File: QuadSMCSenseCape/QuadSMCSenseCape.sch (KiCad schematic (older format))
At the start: 16 parts, among them P8 BeagleBone_Black_Header, P9 BeagleBone_Black_Header, T1 Motor 1, T2 Motor 2, T3 Motor 3, T4 Motor 4, U1 TC4428, U2 TC4428, U3 TC4428, U4 TC4428, U5 74HCT00, U6 74HCT00

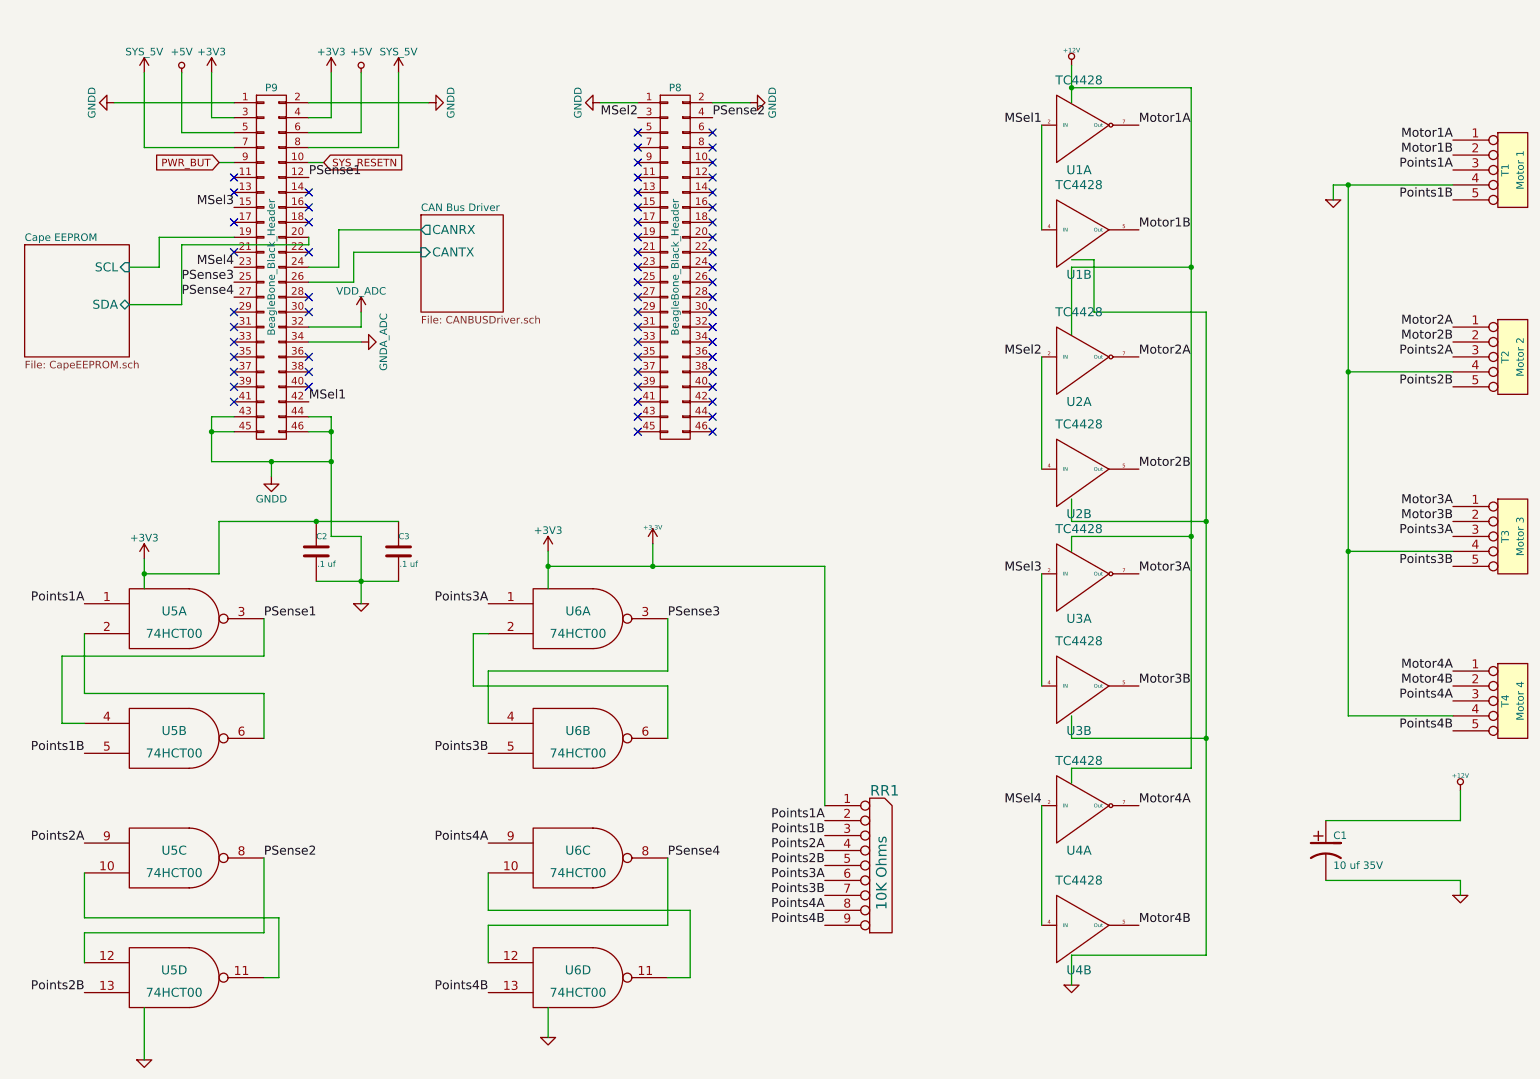
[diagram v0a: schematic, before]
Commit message: Remove CAN bus driver from QuadSMCSenseCape (delegate that to a dedicated Cape).
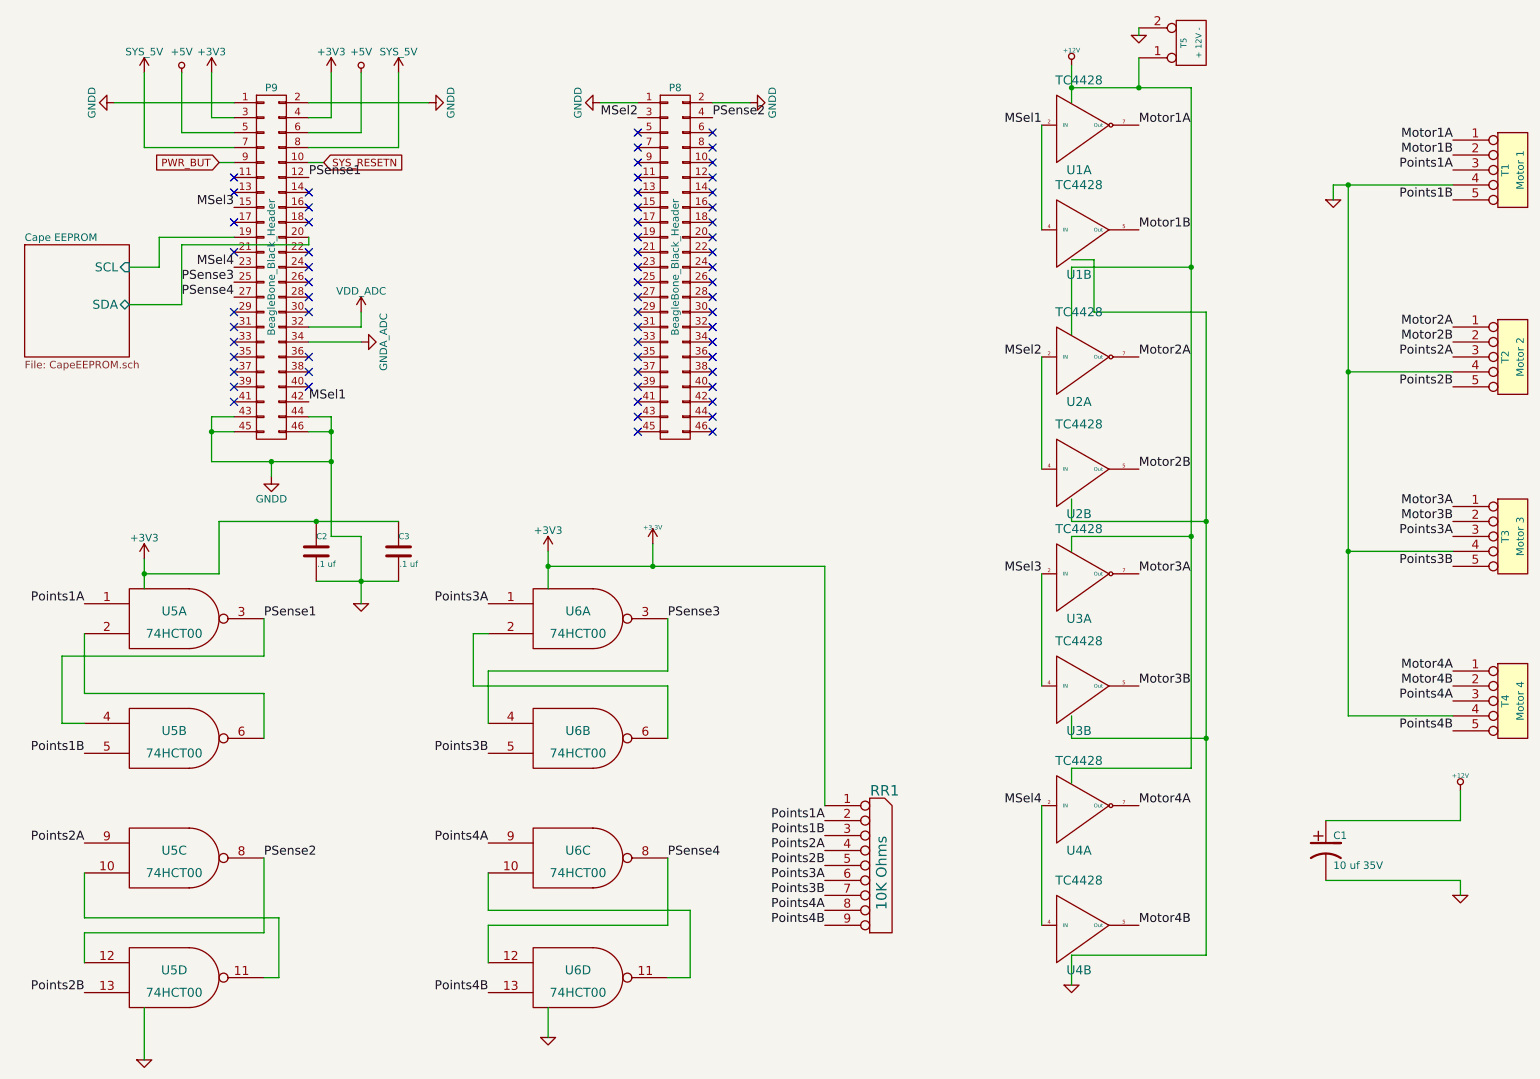
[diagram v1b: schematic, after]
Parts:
- added T5: + 12V -, symbol CONN_2
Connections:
- net +12V: now also T5.1 (P1)
- net GND: now also T5.2 (PM)
- net CAN Bus Driver/CANRX: no longer names the net of P9.24 (P24)
- net CAN Bus Driver/CANTX: no longer names the net of P9.26 (P26)
- no-connect marks 62 -> 64
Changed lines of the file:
@@
 $Descr A4 11693 8268
 encoding utf-8
-Sheet 1 3
+Sheet 1 2
 Title ""
-Date "3 feb 2019"
+Date "23 feb 2019"
 Rev ""
 Comp ""
@@
 	2850 3250 2850 4050
 Wire Wire Line
-	2850 3550 2050 3550
-Wire Wire Line
-	2050 3550 2050 3250
+	2050 3550 2850 3550
+Wire Wire Line
+	2050 3250 2050 3550
 Wire Wire Line
 	2050 3250 2200 3250
@@
 $EndComp
 Wire Wire Line
-	10350 1700 9550 1700
+	9550 1700 10350 1700
 Wire Wire Line
 	9550 1700 9550 1800
@@
 Text Label 6150 6650 2    60   ~ 0
 Points4B
-$Sheet
-S 3450 1900 550  650
-U 5C572C55
-F0 "CAN Bus Driver" 50
-F1 "CANBUSDriver.sch" 50
-F2 "CANTX" I L 3450 2150 60
-F3 "CANRX" O L 3450 2000 60
-$EndSheet
 Wire Wire Line
 	10400 5950 10400 5750
@@
 Text Label 5400 1250 0    60   ~ 0
 PSense2
-Wire Wire Line
-	3450 2000 2900 2000
-Wire Wire Line
-	2900 2000 2900 2250
-Wire Wire Line
-	2900 2250 2700 2250
-Wire Wire Line
-	3450 2150 3000 2150
-Wire Wire Line
-	3000 2150 3000 2350
-Wire Wire Line
-	3000 2350 2700 2350
 $Sheet
 S 800  2100 700  750
@@
 	1    0    0    -1
 $EndComp
+NoConn ~ 2700 2250
+NoConn ~ 2700 2350
+$Comp
+L CONN_2 T5
+U 1 1 5C7149FE
+P 8600 750
+F 0 "T5" V 8550 750 40  0000 C CNN
+F 1 "+ 12V -" V 8650 750 40  0000 C CNN
+F 2 "" H 8600 750 60  0000 C CNN
+F 3 "" H 8600 750 60  0000 C CNN
+	1    8600 750
+	1    0    0    1
+$EndComp
+Wire Wire Line
+	8250 850  8250 1050
+Connection ~ 8250 1050
+$Comp
+L GND #PWR025
+U 1 1 5C714AB7
+P 8250 700
+F 0 "#PWR025" H 8250 700 30  0001 C CNN
+F 1 "GND" H 8250 630 30  0001 C CNN
+F 2 "" H 8250 700 60  0000 C CNN
+F 3 "" H 8250 700 60  0000 C CNN
+	1    8250 700
+	1    0    0    -1
+$EndComp
+Wire Wire Line
+	8250 650  8250 700
 $EndSCHEMATC

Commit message: Create BOM for QuadSMCSenseCape.
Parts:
- C1: Mouser Part Number (none) -> 667-ECA-1HM100I
- C2, C3: Mouser Part Number (none) -> 581-SR201C104KARTR1
- P8, P9: Mouser Part Number (none) -> 200-ESQ12314GD
- RR1: Mouser Part Number (none) -> 652-4609X-1LF-10K
- T1, T2, T3, T4: Mouser Part Number (none) -> 651-1725685
- T5: Mouser Part Number (none) -> 651-1725656
- U1, U2, U3, U4: Mouser Part Number (none) -> 579-TC4428VPA
- U5, U6: Mouser Part Number (none) -> 595-SN74AHC00N
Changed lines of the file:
@@
 Sheet 1 2
 Title ""
-Date "23 feb 2019"
+Date "12 mar 2019"
 Rev ""
 Comp ""
@@
 F 2 "Socket_BeagleBone_Black:Socket_BeagleBone_Black" H 2450 1400 60  0001 C CNN
 F 3 "" H 2450 1400 60  0000 C CNN
+F 4 "200-ESQ12314GD " H 2450 2250 60  0001 C CNN "Mouser Part Number"
 	1    2450 2250
 	1    0    0    -1
@@
 F 2 "Socket_BeagleBone_Black:Socket_BeagleBone_Black" H 5150 1400 60  0001 C CNN
 F 3 "" H 5150 1400 60  0000 C CNN
+F 4 "200-ESQ12314GD " H 5150 2250 60  0001 C CNN "Mouser Part Number"
 	1    5150 2250
 	1    0    0    -1
@@
 F 2 "~" H 7850 1300 60  0000 C CNN
 F 3 "~" H 7850 1300 60  0000 C CNN
+F 4 "579-TC4428VPA" H 7850 1300 60  0001 C CNN "Mouser Part Number"
 	1    7850 1300
 	1    0    0    -1
@@
 F 2 "~" H 7850 2850 60  0000 C CNN
 F 3 "~" H 7850 2850 60  0000 C CNN
+F 4 "579-TC4428VPA" H 7850 2850 60  0001 C CNN "Mouser Part Number"
 	1    7850 2850
 	1    0    0    -1
@@
 F 2 "~" H 7850 3600 60  0000 C CNN
 F 3 "~" H 7850 3600 60  0000 C CNN
+F 4 "579-TC4428VPA" H 7850 3600 60  0001 C CNN "Mouser Part Number"
 	2    7850 3600
 	1    0    0    -1
@@
 F 2 "~" H 7850 4300 60  0000 C CNN
 F 3 "~" H 7850 4300 60  0000 C CNN
+F 4 "579-TC4428VPA" H 7850 4300 60  0001 C CNN "Mouser Part Number"
 	1    7850 4300
 	1    0    0    -1
@@
 F 2 "~" H 7850 5850 60  0000 C CNN
 F 3 "~" H 7850 5850 60  0000 C CNN
+F 4 "579-TC4428VPA" H 7850 5850 60  0001 C CNN "Mouser Part Number"
 	1    7850 5850
 	1    0    0    -1
@@
 F 2 "" H 10750 1600 60  0000 C CNN
 F 3 "" H 10750 1600 60  0000 C CNN
+F 4 "651-1725685" H 10750 1600 60  0001 C CNN "Mouser Part Number"
 	1    10750 1600
 	1    0    0    -1
@@
 F 2 "" H 10750 2850 60  0000 C CNN
 F 3 "" H 10750 2850 60  0000 C CNN
+F 4 "651-1725685" H 10750 2850 60  0001 C CNN "Mouser Part Number"
 	1    10750 2850
 	1    0    0    -1
@@
 F 2 "" H 10750 4050 60  0000 C CNN
 F 3 "" H 10750 4050 60  0000 C CNN
+F 4 "651-1725685" H 10750 4050 60  0001 C CNN "Mouser Part Number"
 	1    10750 4050
 	1    0    0    -1
@@
 F 2 "" H 10750 5150 60  0000 C CNN
 F 3 "" H 10750 5150 60  0000 C CNN
+F 4 "651-1725685" H 10750 5150 60  0001 C CNN "Mouser Part Number"
 	1    10750 5150
 	1    0    0    -1
@@
 F 2 "~" H 9500 6150 60  0000 C CNN
 F 3 "~" H 9500 6150 60  0000 C CNN
+F 4 "667-ECA-1HM100I" H 9500 6150 60  0001 C CNN "Mouser Part Number"
 	1    9500 6150
 	1    0    0    -1
@@
 F 2 "~" H 1800 4600 60  0000 C CNN
 F 3 "~" H 1800 4600 60  0000 C CNN
+F 4 "595-SN74AHC00N" H 1800 4600 60  0001 C CNN "Mouser Part Number"
 	1    1800 4600
 	1    0    0    -1
@@
 F 2 "~" H 4500 4600 60  0000 C CNN
 F 3 "~" H 4500 4600 60  0000 C CNN
+F 4 "595-SN74AHC00N" H 4500 4600 60  0001 C CNN "Mouser Part Number"
 	1    4500 4600
 	1    0    0    -1
@@
 F 2 "~" H 2788 4000 30  0000 C CNN
 F 3 "~" H 2750 4150 60  0000 C CNN
+F 4 "581-SR201C104KARTR1" H 2750 4150 60  0001 C CNN "Mouser Part Number"
 	1    2750 4150
 	1    0    0    -1
@@
 F 2 "~" H 3338 4000 30  0000 C CNN
 F 3 "~" H 3300 4150 60  0000 C CNN
+F 4 "581-SR201C104KARTR1" H 3300 4150 60  0001 C CNN "Mouser Part Number"
 	1    3300 4150
 	1    0    0    -1
@@
 F 2 "~" H 6500 6300 60  0000 C CNN
 F 3 "~" H 6500 6300 60  0000 C CNN
+F 4 "652-4609X-1LF-10K" H 6500 6300 60  0001 C CNN "Mouser Part Number"
 	1    6500 6300
 	1    0    0    -1
@@
 F 2 "" H 8600 750 60  0000 C CNN
 F 3 "" H 8600 750 60  0000 C CNN
+F 4 "651-1725656" H 8600 750 60  0001 C CNN "Mouser Part Number"
 	1    8600 750
 	1    0    0    1
